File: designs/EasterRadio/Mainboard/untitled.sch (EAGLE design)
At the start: 53 parts, among them IC1 74HC595D, IC2 74HC595D, IC3 74HC595D, IC4 Analog Digital

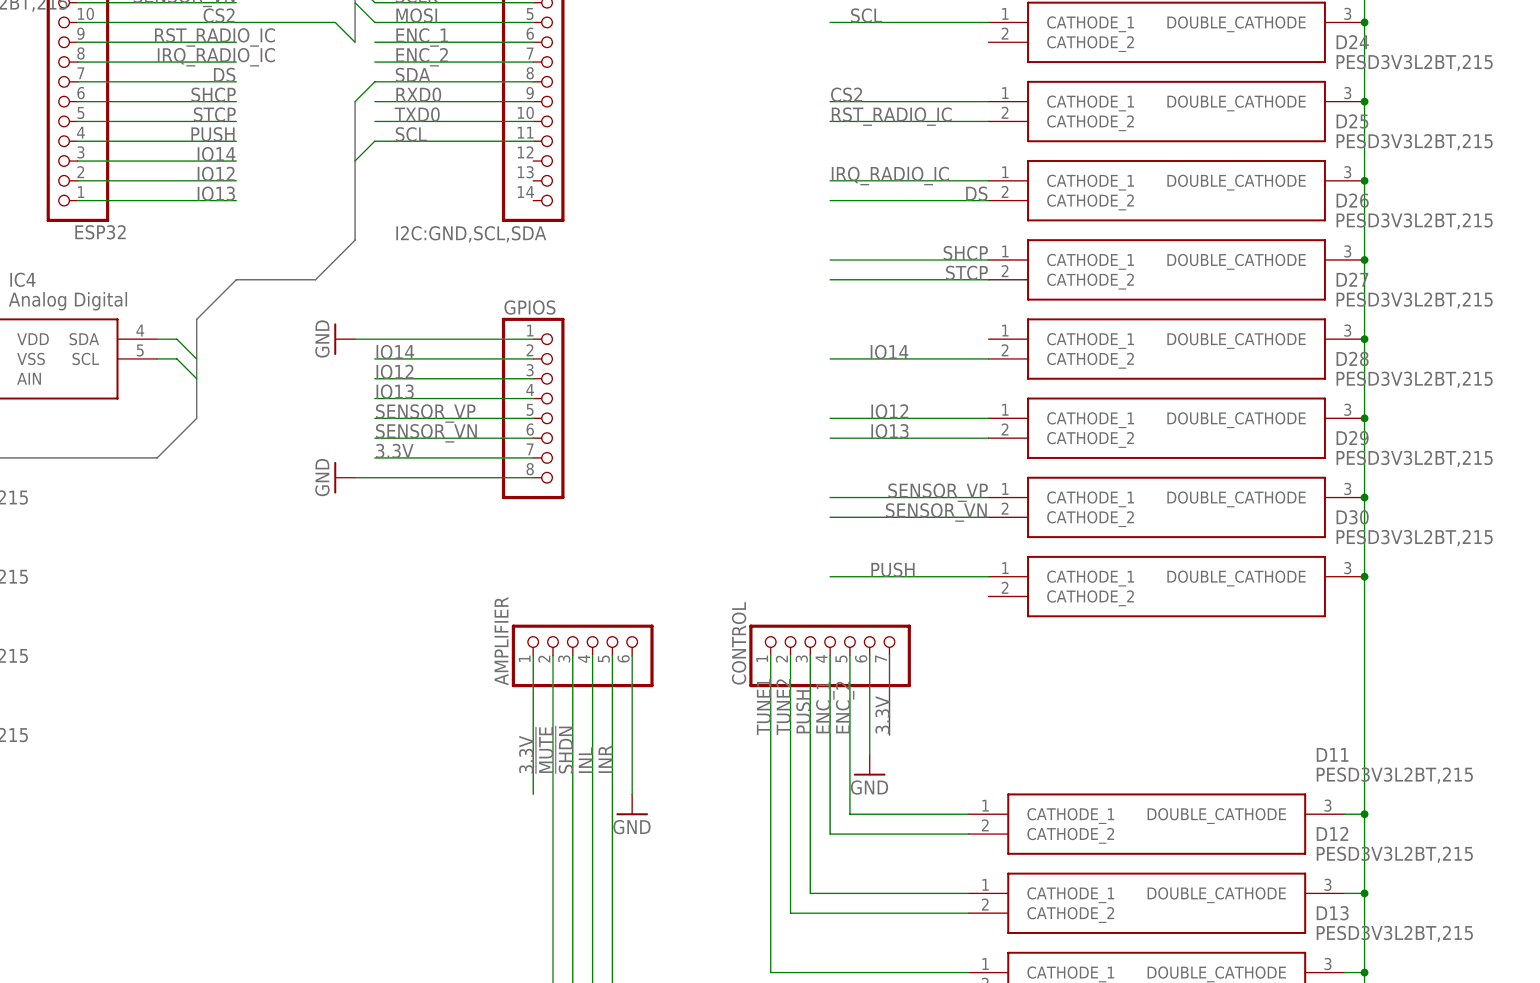
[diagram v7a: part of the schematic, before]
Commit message: changes for new design including swap for amplifier
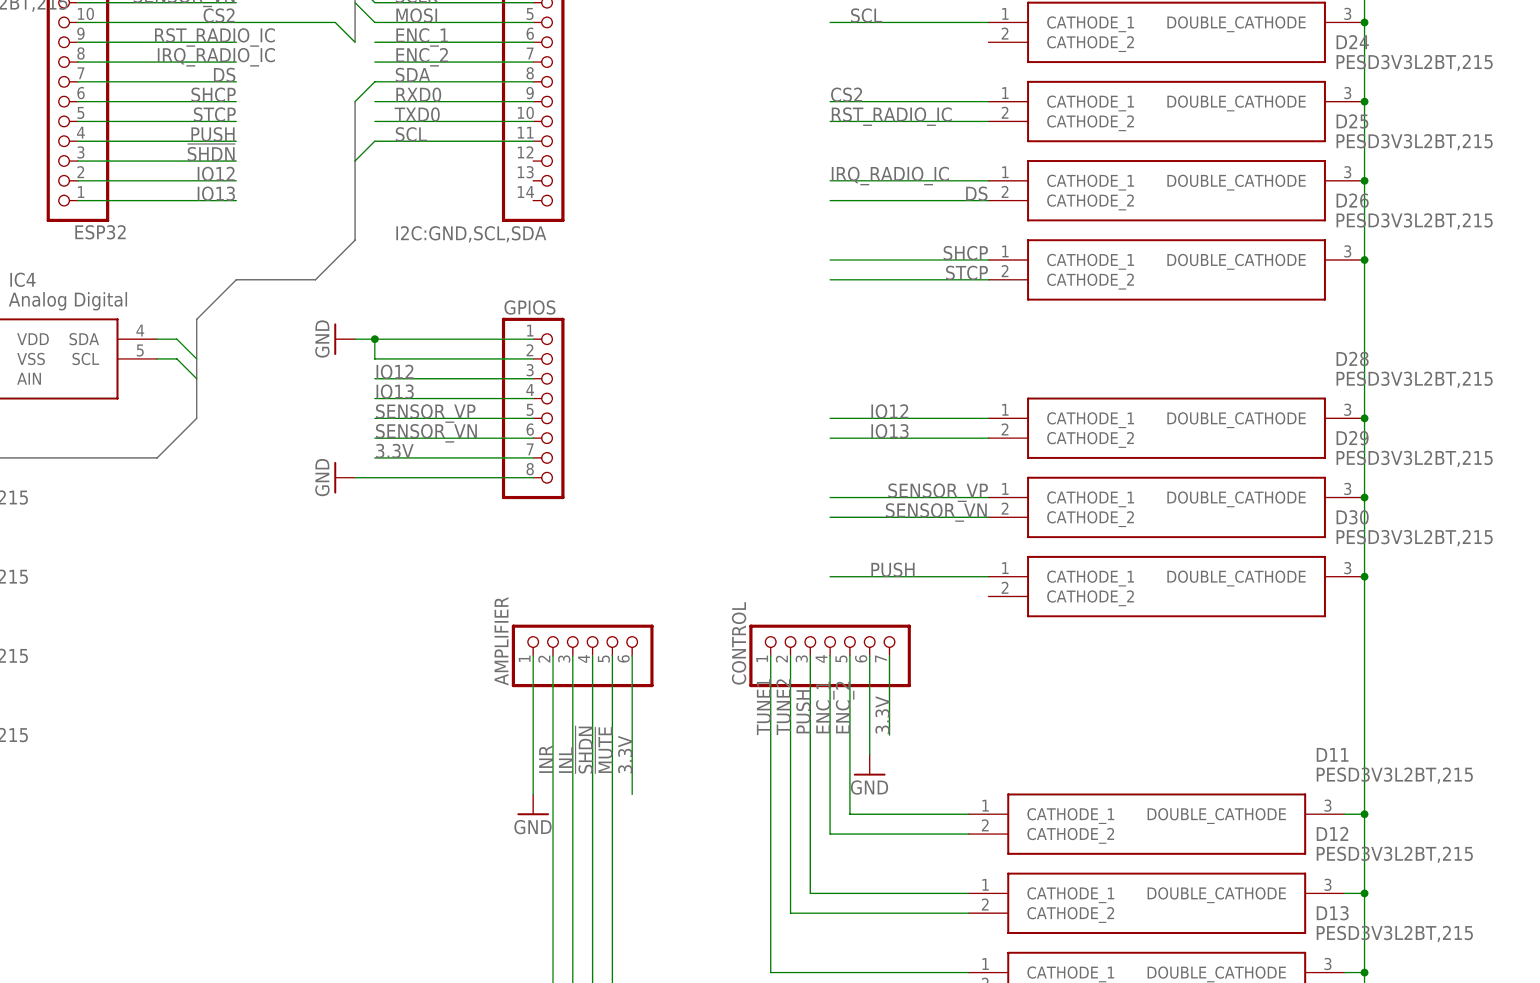
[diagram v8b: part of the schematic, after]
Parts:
- removed D27: PESD3V3L2BT,215, MouserUseful:PESD3V3L2BT,215
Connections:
- removed net IO14: D27.CATHODE_2, ESP32.3, GPIOS.2
- net !MUTE: now also AMPLIFIER.5, D14.CATHODE_1; no longer AMPLIFIER.2, D15.CATHODE_2
- net !SHDN: now also AMPLIFIER.4, D14.CATHODE_2, ESP32.3; no longer AMPLIFIER.3, D15.CATHODE_1
- net 3.3V: now also AMPLIFIER.6; no longer AMPLIFIER.1
- net GND: now also AMPLIFIER.1, GPIOS.2; no longer AMPLIFIER.6, D27.DOUBLE_CATHODE
- net INL: now also AMPLIFIER.3, D15.CATHODE_1; no longer AMPLIFIER.4, D14.CATHODE_2
- net INR: now also AMPLIFIER.2, D15.CATHODE_2; no longer AMPLIFIER.5, D14.CATHODE_1
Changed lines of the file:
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@@
 <part name="D4" library="CommonParts" deviceset="LSM115JE3_TR13" device=""/>
 <part name="GND6" library="supply1" library_urn="urn:adsk.eagle:library:371" deviceset="GND" device=""/>
-<part name="GND4" library="supply1" library_urn="urn:adsk.eagle:library:371" deviceset="GND" device=""/>
 <part name="ENERGY" library="MouserUseful" deviceset="KMMX-BSMT35S-B30TR" device=""/>
 <part name="GND8" library="supply1" library_urn="urn:adsk.eagle:library:371" deviceset="GND" device=""/>
@@
 <part name="D25" library="MouserUseful" deviceset="PESD3V3L2BT,215" device=""/>
 <part name="D26" library="MouserUseful" deviceset="PESD3V3L2BT,215" device=""/>
-<part name="D27" library="MouserUseful" deviceset="PESD3V3L2BT,215" device=""/>
 <part name="D28" library="MouserUseful" deviceset="PESD3V3L2BT,215" device=""/>
 <part name="D29" library="MouserUseful" deviceset="PESD3V3L2BT,215" device=""/>
@@
 <part name="R2" library="rcl" library_urn="urn:adsk.eagle:library:334" deviceset="R-EU_" device="R0805" package3d_urn="urn:adsk.eagle:package:23553/2" value="10K"/>
 <part name="GND3" library="supply1" library_urn="urn:adsk.eagle:library:371" deviceset="GND" device=""/>
+<part name="GND4" library="supply1" library_urn="urn:adsk.eagle:library:371" deviceset="GND" device=""/>
 </parts>
 <sheets>
@@
 <attribute name="VALUE" x="68.58" y="76.2" size="1.778" layer="96"/>
 </instance>
-<instance part="GND4" gate="1" x="251.46" y="63.5" smashed="yes">
-<attribute name="VALUE" x="248.92" y="60.96" size="1.778" layer="96"/>
-</instance>
 <instance part="ENERGY" gate="G$1" x="86.36" y="137.16" smashed="yes">
 <attribute name="NAME" x="105.41" y="144.78" size="1.778" layer="95" align="center-left"/>
@@
 <attribute name="VALUE" x="341.63" y="139.7" size="1.778" layer="96" align="center-left"/>
 </instance>
-<instance part="D27" gate="G$1" x="297.18" y="124.46" smashed="yes">
-<attribute name="NAME" x="341.63" y="132.08" size="1.778" layer="95" align="center-left"/>
-<attribute name="VALUE" x="341.63" y="129.54" size="1.778" layer="96" align="center-left"/>
-</instance>
 <instance part="D28" gate="G$1" x="297.18" y="114.3" smashed="yes">
 <attribute name="NAME" x="341.63" y="121.92" size="1.778" layer="95" align="center-left"/>
@@
 <instance part="GND3" gate="1" x="129.54" y="114.3" smashed="yes">
 <attribute name="VALUE" x="127" y="111.76" size="1.778" layer="96"/>
+</instance>
+<instance part="GND4" gate="1" x="238.76" y="63.5" smashed="yes">
+<attribute name="VALUE" x="236.22" y="60.96" size="1.778" layer="96"/>
 </instance>
 </instances>
@@
 <wire x1="241.3" y1="233.68" x2="241.3" y2="254" width="0.1524" layer="91"/>
 <label x="241.3" y="251.46" size="1.778" layer="95" rot="R90" align="bottom-right"/>
-</segment>
-<segment>
-<pinref part="AMPLIFIER" gate="A" pin="1"/>
-<wire x1="238.76" y1="83.82" x2="238.76" y2="66.04" width="0.1524" layer="91"/>
-<label x="238.76" y="68.58" size="1.778" layer="95" rot="R90"/>
 </segment>
 <segment>
@@
 <wire x1="284.48" y1="83.82" x2="284.48" y2="73.66" width="0.1524" layer="91"/>
 <label x="284.48" y="73.66" size="1.778" layer="95" rot="R90"/>
+</segment>
+<segment>
+<pinref part="AMPLIFIER" gate="A" pin="6"/>
+<wire x1="251.46" y1="83.82" x2="251.46" y2="66.04" width="0.1524" layer="91"/>
+<label x="251.46" y="68.58" size="1.778" layer="95" rot="R90"/>
 </segment>
 </net>
@@
 <junction x="43.18" y="93.98"/>
 <junction x="71.12" y="93.98"/>
-</segment>
-<segment>
-<pinref part="AMPLIFIER" gate="A" pin="6"/>
-<wire x1="251.46" y1="83.82" x2="251.46" y2="66.04" width="0.1524" layer="91"/>
-<pinref part="GND4" gate="1" pin="GND"/>
 </segment>
 <segment>
@@
 <pinref part="D28" gate="G$1" pin="DOUBLE_CATHODE"/>
 <wire x1="345.44" y1="104.14" x2="345.44" y2="114.3" width="0.1524" layer="91"/>
-<pinref part="D27" gate="G$1" pin="DOUBLE_CATHODE"/>
-<wire x1="345.44" y1="114.3" x2="345.44" y2="124.46" width="0.1524" layer="91"/>
 <junction x="345.44" y="114.3"/>
 <pinref part="D26" gate="G$1" pin="DOUBLE_CATHODE"/>
-<wire x1="345.44" y1="124.46" x2="345.44" y2="134.62" width="0.1524" layer="91"/>
-<junction x="345.44" y="124.46"/>
+<wire x1="345.44" y1="114.3" x2="345.44" y2="134.62" width="0.1524" layer="91"/>
 <pinref part="D25" gate="G$1" pin="DOUBLE_CATHODE"/>
 <wire x1="345.44" y1="134.62" x2="345.44" y2="144.78" width="0.1524" layer="91"/>
@@
 </segment>
 <segment>
-<wire x1="238.76" y1="124.46" x2="215.9" y2="124.46" width="0.1524" layer="91"/>
+<wire x1="238.76" y1="124.46" x2="218.44" y2="124.46" width="0.1524" layer="91"/>
 <pinref part="GPIOS" gate="A" pin="1"/>
 <pinref part="GND19" gate="1" pin="GND"/>
+<wire x1="218.44" y1="124.46" x2="215.9" y2="124.46" width="0.1524" layer="91"/>
+<wire x1="238.76" y1="121.92" x2="218.44" y2="121.92" width="0.1524" layer="91"/>
+<pinref part="GPIOS" gate="A" pin="2"/>
+<wire x1="218.44" y1="121.92" x2="218.44" y2="124.46" width="0.1524" layer="91"/>
+<junction x="218.44" y="124.46"/>
 </segment>
 <segment>
@@
 <pinref part="GND3" gate="1" pin="GND"/>
 </segment>
+<segment>
+<pinref part="AMPLIFIER" gate="A" pin="1"/>
+<wire x1="238.76" y1="83.82" x2="238.76" y2="66.04" width="0.1524" layer="91"/>
+<pinref part="GND4" gate="1" pin="GND"/>
+</segment>
 </net>
 <net name="RXD0" class="1">
@@
 </segment>
 </net>
-<net name="IO14" class="0">
-<segment>
-<pinref part="ESP32" gate="A" pin="3"/>
-<wire x1="180.34" y1="147.32" x2="200.66" y2="147.32" width="0.1524" layer="91"/>
-<label x="200.66" y="147.32" size="1.778" layer="95" align="bottom-right"/>
-</segment>
-<segment>
-<wire x1="238.76" y1="121.92" x2="218.44" y2="121.92" width="0.1524" layer="91"/>
-<label x="218.44" y="121.92" size="1.778" layer="95" rot="R180" align="top-right"/>
-<pinref part="GPIOS" gate="A" pin="2"/>
-</segment>
-<segment>
-<wire x1="276.86" y1="121.92" x2="297.18" y2="121.92" width="0.1524" layer="91"/>
-<label x="287.02" y="121.92" size="1.778" layer="95" align="bottom-right"/>
-<pinref part="D27" gate="G$1" pin="CATHODE_2"/>
-</segment>
-</net>
 <net name="CS2" class="0">
 <segment>
@@
 </net>
 <net name="INR" class="0">
-<segment>
-<pinref part="AMPLIFIER" gate="A" pin="5"/>
-<label x="248.92" y="68.58" size="1.778" layer="95" rot="R90"/>
-<wire x1="248.92" y1="83.82" x2="248.92" y2="33.02" width="0.1524" layer="91"/>
-<pinref part="D14" gate="G$1" pin="CATHODE_1"/>
-<wire x1="294.64" y1="33.02" x2="248.92" y2="33.02" width="0.1524" layer="91"/>
-</segment>
 <segment>
 <pinref part="STEREO" gate="G$1" pin="RING"/>
@@
 <wire x1="88.9" y1="78.74" x2="109.22" y2="78.74" width="0.1524" layer="91"/>
 </segment>
+<segment>
+<pinref part="AMPLIFIER" gate="A" pin="2"/>
+<label x="241.3" y="68.58" size="1.778" layer="95" rot="R90"/>
+<wire x1="241.3" y1="83.82" x2="241.3" y2="20.32" width="0.1524" layer="91"/>
+<pinref part="D15" gate="G$1" pin="CATHODE_2"/>
+<wire x1="294.64" y1="20.32" x2="241.3" y2="20.32" width="0.1524" layer="91"/>
+</segment>
 </net>
 <net name="INL" class="0">
-<segment>
-<pinref part="AMPLIFIER" gate="A" pin="4"/>
-<label x="246.38" y="68.58" size="1.778" layer="95" rot="R90"/>
-<wire x1="246.38" y1="83.82" x2="246.38" y2="30.48" width="0.1524" layer="91"/>
-<pinref part="D14" gate="G$1" pin="CATHODE_2"/>
-<wire x1="294.64" y1="30.48" x2="246.38" y2="30.48" width="0.1524" layer="91"/>
-</segment>
 <segment>
 <pinref part="STEREO" gate="G$1" pin="TIP"/>
@@
 <wire x1="109.22" y1="76.2" x2="91.44" y2="76.2" width="0.1524" layer="91"/>
 </segment>
-</net>
-<net name="!MUTE" class="0">
-<segment>
-<pinref part="AMPLIFIER" gate="A" pin="2"/>
-<label x="241.3" y="68.58" size="1.778" layer="95" rot="R90"/>
-<wire x1="241.3" y1="83.82" x2="241.3" y2="20.32" width="0.1524" layer="91"/>
-<pinref part="D15" gate="G$1" pin="CATHODE_2"/>
-<wire x1="294.64" y1="20.32" x2="241.3" y2="20.32" width="0.1524" layer="91"/>
-</segment>
-</net>
-<net name="!SHDN" class="0">
 <segment>
 <pinref part="AMPLIFIER" gate="A" pin="3"/>
@@
 </segment>
 </net>
+<net name="!MUTE" class="0">
+<segment>
+<pinref part="AMPLIFIER" gate="A" pin="5"/>
+<label x="248.92" y="68.58" size="1.778" layer="95" rot="R90"/>
+<wire x1="248.92" y1="83.82" x2="248.92" y2="33.02" width="0.1524" layer="91"/>
+<pinref part="D14" gate="G$1" pin="CATHODE_1"/>
+<wire x1="294.64" y1="33.02" x2="248.92" y2="33.02" width="0.1524" layer="91"/>
+</segment>
+</net>
+<net name="!SHDN" class="0">
+<segment>
+<pinref part="AMPLIFIER" gate="A" pin="4"/>
+<label x="246.38" y="68.58" size="1.778" layer="95" rot="R90"/>
+<wire x1="246.38" y1="83.82" x2="246.38" y2="30.48" width="0.1524" layer="91"/>
+<pinref part="D14" gate="G$1" pin="CATHODE_2"/>
+<wire x1="294.64" y1="30.48" x2="246.38" y2="30.48" width="0.1524" layer="91"/>
+</segment>
+<segment>
+<pinref part="ESP32" gate="A" pin="3"/>
+<wire x1="180.34" y1="147.32" x2="200.66" y2="147.32" width="0.1524" layer="91"/>
+<label x="200.66" y="147.32" size="1.778" layer="95" align="bottom-right"/>
+</segment>
+</net>
